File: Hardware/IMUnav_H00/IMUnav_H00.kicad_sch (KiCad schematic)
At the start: 39 parts, among them J1 Conn_01x03_Pin, J2 Conn_01x03_Pin, J3 Conn_01x03_Pin, J4 Conn_01x03_Pin, J5 Conn_01x03_Pin, J6 Conn_01x03_Pin, U1 STM32F446VETx, X1 SX5M24.000M20F30TNN

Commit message: PCB routing
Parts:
- removed J1: Conn_01x03_Pin, Connector_PinHeader_2.54mm:PinHeader_1x03_P2.54mm_Vertical, symbol Connector:Conn_01x03_Pin
- added J10: Conn_ARM_JTAG_SWD_10, Connector_PinHeader_1.27mm:PinHeader_2x05_P1.27mm_Vertical, symbol Connector:Conn_ARM_JTAG_SWD_10
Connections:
- new net: J10.3 (GND), J10.5 (GND)
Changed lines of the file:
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@@
   (junction (at 64.77 106.68) (diameter 0) (color 0 0 0 0)
   )
-  (junction (at 73.66 106.68) (diameter 0) (color 0 0 0 0)
-  )
   (junction (at 203.2 67.31) (diameter 0) (color 0 0 0 0)
   )
@@
   (junction (at 187.96 134.62) (diameter 0) (color 0 0 0 0)
   )
-  (junction (at 71.12 104.14) (diameter 0) (color 0 0 0 0)
-  )
   (junction (at 219.71 35.56) (diameter 0) (color 0 0 0 0)
   )
@@
   (no_connect (at 152.4 158.75))
   (no_connect (at 106.68 80.01))
-  (wire (pts (xy 78.74 93.98) (xy 71.12 93.98))
-    (stroke (width 0) (type default))
-  )
   (wire (pts (xy 276.86 34.29) (xy 276.86 16.51))
     (stroke (width 0) (type default))
@@
     (stroke (width 0) (type default))
   )
-  (wire (pts (xy 73.66 96.52) (xy 73.66 106.68))
-    (stroke (width 0) (type default))
-  )
   (wire (pts (xy 152.4 107.95) (xy 156.21 107.95))
     (stroke (width 0) (type default))
@@
     (stroke (width 0) (type default))
   )
-  (wire (pts (xy 73.66 106.68) (xy 64.77 106.68))
-    (stroke (width 0) (type default))
-  )
   (wire (pts (xy 262.89 88.9) (xy 273.05 88.9))
     (stroke (width 0) (type default))
@@
     (stroke (width 0) (type default))
   )
+  (wire (pts (xy 262.89 49.53) (xy 270.51 49.53))
+    (stroke (width 0) (type default))
+  )
   (wire (pts (xy 198.12 81.28) (xy 203.2 81.28))
     (stroke (width 0) (type default))
@@
     (stroke (width 0) (type default))
   )
-  (wire (pts (xy 71.12 104.14) (xy 76.2 104.14))
-    (stroke (width 0) (type default))
-  )
   (wire (pts (xy 191.77 88.9) (xy 205.74 88.9))
     (stroke (width 0) (type default))
@@
     (stroke (width 0) (type default))
   )
-  (wire (pts (xy 262.89 25.4) (xy 270.51 25.4))
-    (stroke (width 0) (type default))
-  )
   (wire (pts (xy 187.96 134.62) (xy 196.85 134.62))
     (stroke (width 0) (type default))
   )
-  (wire (pts (xy 262.89 49.53) (xy 270.51 49.53))
-    (stroke (width 0) (type default))
-  )
   (wire (pts (xy 220.98 143.51) (xy 224.79 143.51))
     (stroke (width 0) (type default))
   )
-  (wire (pts (xy 71.12 93.98) (xy 71.12 104.14))
-    (stroke (width 0) (type default))
-  )
   (wire (pts (xy 77.47 176.53) (xy 95.25 176.53))
     (stroke (width 0) (type default))
@@
     (stroke (width 0) (type default))
   )
-  (wire (pts (xy 76.2 97.79) (xy 78.74 97.79))
-    (stroke (width 0) (type default))
-  )
   (wire (pts (xy 220.98 99.06) (xy 224.79 99.06))
     (stroke (width 0) (type default))
@@
     (stroke (width 0) (type default))
   )
-  (wire (pts (xy 73.66 106.68) (xy 76.2 106.68))
+  (wire (pts (xy 64.77 106.68) (xy 76.2 106.68))
     (stroke (width 0) (type default))
   )
@@
     (stroke (width 0) (type default))
   )
-  (wire (pts (xy 71.12 104.14) (xy 57.15 104.14))
-    (stroke (width 0) (type default))
-  )
-  (wire (pts (xy 78.74 97.79) (xy 78.74 99.06))
+  (wire (pts (xy 57.15 104.14) (xy 76.2 104.14))
     (stroke (width 0) (type default))
   )
@@
     (stroke (width 0) (type default))
   )
-  (wire (pts (xy 78.74 96.52) (xy 73.66 96.52))
-    (stroke (width 0) (type default))
-  )
   (wire (pts (xy 121.92 13.97) (xy 121.92 31.75))
     (stroke (width 0) (type default))
@@
     (stroke (width 0) (type default))
   )
+  (wire (pts (xy 262.89 52.07) (xy 267.97 52.07))
+    (stroke (width 0) (type default))
+  )
   (wire (pts (xy 190.5 132.08) (xy 185.42 132.08))
     (stroke (width 0) (type default))
@@
     (stroke (width 0) (type default))
   )
-  (wire (pts (xy 262.89 27.94) (xy 270.51 27.94))
-    (stroke (width 0) (type default))
-  )
   (wire (pts (xy 102.87 135.89) (xy 106.68 135.89))
     (stroke (width 0) (type default))
@@
     (stroke (width 0) (type default))
   )
+  (wire (pts (xy 262.89 27.94) (xy 270.51 27.94))
+    (stroke (width 0) (type default))
+  )
   (wire (pts (xy 152.4 46.99) (xy 156.21 46.99))
     (stroke (width 0) (type default))
@@
     (stroke (width 0) (type default))
   )
+  (wire (pts (xy 262.89 25.4) (xy 270.51 25.4))
+    (stroke (width 0) (type default))
+  )
   (wire (pts (xy 152.4 52.07) (xy 156.21 52.07))
     (stroke (width 0) (type default))
@@
     (stroke (width 0) (type default))
   )
-  (wire (pts (xy 267.97 52.07) (xy 262.89 52.07))
-    (stroke (width 0) (type default))
-  )
   (wire (pts (xy 203.2 38.1) (xy 200.66 38.1))
     (stroke (width 0) (type default))
@@
     )
   )
+  (symbol (lib_id "Connector:Conn_ARM_JTAG_SWD_10") (at -77.47 142.24 0) (unit 1)
+    (in_bom yes) (on_board yes) (dnp no) (fields_autoplaced)
+    (property "Reference" "J10" (at -88.3919 141.0279 0)
+      (effects (font (size 1.27 1.27)) (justify right))
+    )
+    (property "Value" "Conn_ARM_JTAG_SWD_10" (at -88.3919 143.4521 0)
+      (effects (font (size 1.27 1.27)) (justify right))
+    )
+    (property "Footprint" "Connector_PinHeader_1.27mm:PinHeader_2x05_P1.27mm_Vertical" (at -77.47 142.24 0)
+      (effects (font (size 1.27 1.27)) hide)
+    )
+    (property "Datasheet" "http://infocenter.arm.com/help/topic/com.arm.doc.ddi0314h/DDI0314H_coresight_components_trm.pdf" (at -86.36 173.99 90)
+      (effects (font (size 1.27 1.27)) hide)
+    )
+    (pin "9")
+    (pin "2")
+    (pin "4")
+    (pin "7")
+    (pin "8")
+    (pin "10")
+    (pin "1")
+    (pin "3")
+    (pin "5")
+    (pin "6")
+    (instances
+      (project "IMUnav_H00"
+        (path "/4c2dd95e-3649-4040-ab57-00df6d22e0b0"
+          (reference "J10") (unit 1)
+        )
+      )
+    )
+  )
   (symbol (lib_id "Device:R") (at 204.47 127 0) (mirror y) (unit 1)
     (in_bom yes) (on_board yes) (dnp no)
@@
     )
   )
-  (symbol (lib_id "power:GND") (at 76.2 97.79 0) (mirror y) (unit 1)
-    (in_bom yes) (on_board yes) (dnp no)
-    (property "Reference" "#PWR023" (at 76.2 104.14 0)
-      (effects (font (size 1.27 1.27)) hide)
-    )
-    (property "Value" "GND" (at 76.073 102.1842 0)
-      (effects (font (size 1.27 1.27)))
-    )
-    (property "Footprint" "" (at 76.2 97.79 0)
-      (effects (font (size 1.27 1.27)) hide)
-    )
-    (property "Datasheet" "" (at 76.2 97.79 0)
-      (effects (font (size 1.27 1.27)) hide)
-    )
-    (pin "1")
-    (instances
-      (project "IMUnav_H00"
-        (path "/4c2dd95e-3649-4040-ab57-00df6d22e0b0"
-          (reference "#PWR023") (unit 1)
-        )
-      )
-      (project "PaLampa_MoBo_H01"
-        (path "/68867493-9f89-4388-916e-56f5ada0ac5c"
-          (reference "#PWR?") (unit 1)
-        )
-      )
-    )
-  )
   (symbol (lib_id "Device:R") (at 64.77 97.79 0) (unit 1)
     (in_bom yes) (on_board yes) (dnp no)
@@
     )
   )
-  (symbol (lib_id "Connector:Conn_01x03_Pin") (at 83.82 96.52 0) (mirror y) (unit 1)
-    (in_bom yes) (on_board yes) (dnp no)
-    (property "Reference" "J1" (at 83.185 89.7595 0)
-      (effects (font (size 1.27 1.27)))
-    )
-    (property "Value" "Conn_01x03_Pin" (at 77.47 91.44 0)
-      (effects (font (size 1.27 1.27)))
-    )
-    (property "Footprint" "Connector_PinHeader_2.54mm:PinHeader_1x03_P2.54mm_Vertical" (at 83.82 96.52 0)
-      (effects (font (size 1.27 1.27)) hide)
-    )
-    (property "Datasheet" "~" (at 83.82 96.52 0)
-      (effects (font (size 1.27 1.27)) hide)
-    )
-    (pin "1")
-    (pin "2")
-    (pin "3")
-    (instances
-      (project "IMUnav_H00"
-        (path "/4c2dd95e-3649-4040-ab57-00df6d22e0b0"
-          (reference "J1") (unit 1)
-        )
-      )
-    )
-  )
   (symbol (lib_id "Device:C") (at 41.91 161.29 0) (unit 1)
     (in_bom yes) (on_board yes) (dnp no)
@@
       (effects (font (size 1.27 1.27)) (justify right))
     )
-    (pin "USB1_D+" input (at 262.89 49.53 0)
+    (pin "USB1_D+" input (at 262.89 25.4 0)
       (effects (font (size 1.27 1.27)) (justify right))
     )
-    (pin "USB1_D-" input (at 262.89 52.07 0)
+    (pin "USB1_D-" input (at 262.89 27.94 0)
       (effects (font (size 1.27 1.27)) (justify right))
     )
-    (pin "USB4_D-" input (at 262.89 27.94 0)
+    (pin "USB4_D-" input (at 262.89 52.07 0)
       (effects (font (size 1.27 1.27)) (justify right))
     )
-    (pin "USB4_D+" input (at 262.89 25.4 0)
+    (pin "USB4_D+" input (at 262.89 49.53 0)
       (effects (font (size 1.27 1.27)) (justify right))
     )

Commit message: PCB routing
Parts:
- removed SWD1: Conn_01x06_Pin, Connector_PinHeader_2.54mm:PinHeader_1x06_P2.54mm_Vertical, symbol Connector:Conn_01x06_Pin
- added RESET2: SW_SPST, Button_Switch_SMD:SW_SPST_TL3342, symbol Switch:SW_SPST
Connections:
- net +3V3: now also J10.1 (VTref)
- net GND: now also J10.3 (GND), J10.5 (GND), J10.9 (GNDDetect), RESET2.1 (A)
- net SWD_CLK: now also J10.4 (SWCLK/TCK)
- net SWD_NRST: now also J10.10 (~{RESET}), RESET2.2 (B)
- net SWD_SWIO: now also J10.2 (SWDIO/TMS)
- net SWD_SWO: now also J10.6 (SWO/TDO)
- no-connect marks 21 -> 22
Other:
- moved on the sheet: J10

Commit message: Silkscreen layout
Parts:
- added G1: FEEC_logo, IMUnav:FEEC_logo, symbol IMUnav:FEEC_logo
- added G2: FEEC_logo_long, IMUnav:FEEC_logo_long, symbol IMUnav:FEEC_logo_long
- renumbered J10 to J1, RESET2 to RESET1

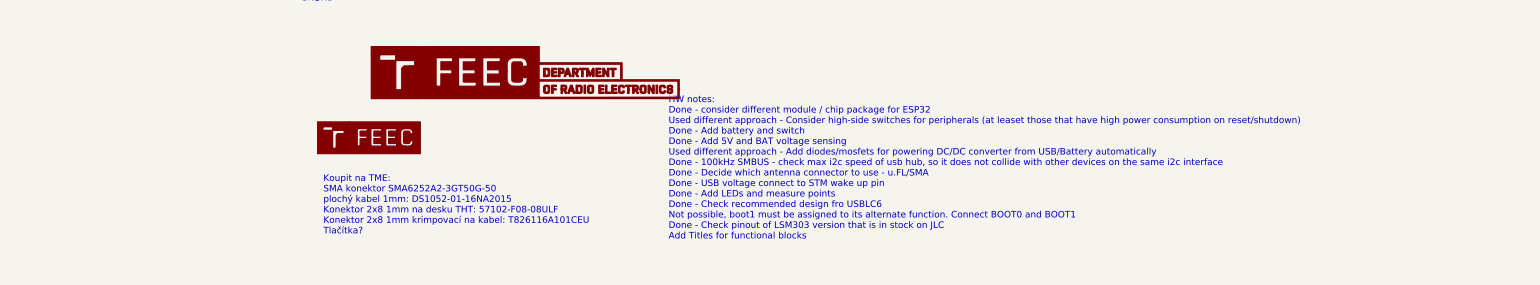
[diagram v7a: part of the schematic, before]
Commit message: PCB touch-ups, bom file for testing
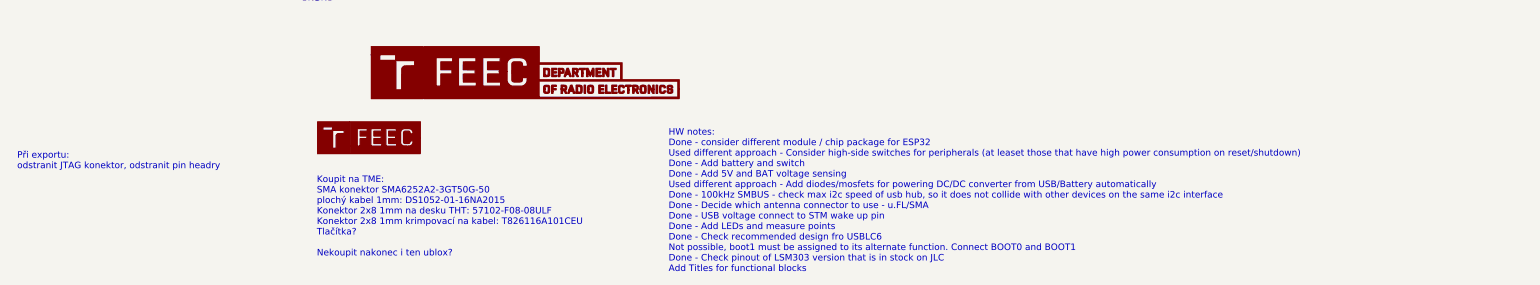
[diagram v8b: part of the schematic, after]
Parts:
- J1, J2, J3, J4, J5, J6: now left out of the parts list
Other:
- note added: "Koupit na TME: SMA konektor SMA6252A2-3GT50G-50 plochý kabel 1mm: DS1052-01-16NA2015 Konektor 2x8 1mm na desku THT: 57102-F08-08ULF Konektor 2x8 1mm krimpovací na kabel: T826116A101CEU Tlačítka? Nekoupit nakonec i ten ublox?"
- note added: "Při exportu: odstranit JTAG konektor, odstranit pin headry"
- note removed: "Koupit na TME: SMA konektor SMA6252A2-3GT50G-50 plochý kabel 1mm: DS1052-01-16NA2015 Konektor 2x8 1mm na desku THT: 57102-F08-08ULF Konektor 2x8 1mm krimpovací na kabel: T826116A101CEU Tlačítka?"
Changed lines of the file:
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@@
     (stroke (width 0) (type default))
   )
+  (text "Při exportu:\nodstranit JTAG konektor, odstranit pin headry"
+    (at 15.24 229.87 0)
+    (effects (font (size 1.27 1.27)) (justify left bottom))
+  )
   (text "HW notes:\nDone - consider different module / chip package for ESP32\nUsed different approach - Consider high-side switches for peripherals (at leaset those that have high power consumption on reset/shutdown)\nDone - Add battery and switch\nDone - Add 5V and BAT voltage sensing\nUsed different approach - Add diodes/mosfets for powering DC/DC converter from USB/Battery automatically\nDone - 100kHz SMBUS - check max i2c speed of usb hub, so it does not collide with other devices on the same i2c interface\nDone - Decide which antenna connector to use - u.FL/SMA\nDone - USB voltage connect to STM wake up pin\nDone - Add LEDs and measure points\nDone - Check recommended design fro USBLC6\nNot possible, boot1 must be assigned to its alternate function. Connect BOOT0 and BOOT1\nDone - Check pinout of LSM303 version that is in stock on JLC\nAdd Titles for functional blocks\n\n\n"
-    (at 142.24 247.65 0)
+    (at 142.24 254 0)
     (effects (font (size 1.27 1.27)) (justify left bottom))
   )
-  (text "Koupit na TME:\nSMA konektor SMA6252A2-3GT50G-50\nplochý kabel 1mm: DS1052-01-16NA2015\nKonektor 2x8 1mm na desku THT: 57102-F08-08ULF\nKonektor 2x8 1mm krimpovací na kabel: T826116A101CEU\nTlačítka?\n"
-    (at 74.93 242.57 0)
+  (text "Koupit na TME:\nSMA konektor SMA6252A2-3GT50G-50\nplochý kabel 1mm: DS1052-01-16NA2015\nKonektor 2x8 1mm na desku THT: 57102-F08-08ULF\nKonektor 2x8 1mm krimpovací na kabel: T826116A101CEU\nTlačítka?\n\nNekoupit nakonec i ten ublox?\n\n"
+    (at 73.66 248.92 0)
     (effects (font (size 1.27 1.27)) (justify left bottom))
   )
@@
   )
   (symbol (lib_id "Connector:Conn_ARM_JTAG_SWD_10") (at 74.93 176.53 0) (unit 1)
-    (in_bom yes) (on_board yes) (dnp no)
+    (in_bom no) (on_board yes) (dnp no)
     (property "Reference" "J1" (at 92.71 182.88 0)
       (effects (font (size 1.27 1.27)) (justify right))
@@
   )
   (symbol (lib_id "Connector:Conn_01x03_Pin") (at 193.04 106.68 0) (unit 1)
-    (in_bom yes) (on_board yes) (dnp no) (fields_autoplaced)
+    (in_bom no) (on_board yes) (dnp no) (fields_autoplaced)
     (property "Reference" "J6" (at 193.675 99.9195 0)
       (effects (font (size 1.27 1.27)))
@@
   )
   (symbol (lib_id "Connector:Conn_01x03_Pin") (at 177.8 124.46 0) (unit 1)
-    (in_bom yes) (on_board yes) (dnp no) (fields_autoplaced)
+    (in_bom no) (on_board yes) (dnp no) (fields_autoplaced)
     (property "Reference" "J2" (at 178.435 117.6995 0)
       (effects (font (size 1.27 1.27)))
@@
   )
   (symbol (lib_id "Connector:Conn_01x03_Pin") (at 193.04 27.94 0) (unit 1)
-    (in_bom yes) (on_board yes) (dnp no) (fields_autoplaced)
+    (in_bom no) (on_board yes) (dnp no) (fields_autoplaced)
     (property "Reference" "J3" (at 193.675 21.1795 0)
       (effects (font (size 1.27 1.27)))
@@
   )
   (symbol (lib_id "Connector:Conn_01x03_Pin") (at 193.04 81.28 0) (unit 1)
-    (in_bom yes) (on_board yes) (dnp no) (fields_autoplaced)
+    (in_bom no) (on_board yes) (dnp no) (fields_autoplaced)
     (property "Reference" "J5" (at 193.675 74.5195 0)
       (effects (font (size 1.27 1.27)))
@@
   )
   (symbol (lib_id "Connector:Conn_01x03_Pin") (at 193.04 57.15 0) (unit 1)
-    (in_bom yes) (on_board yes) (dnp no) (fields_autoplaced)
+    (in_bom no) (on_board yes) (dnp no) (fields_autoplaced)
     (property "Reference" "J4" (at 193.675 50.3895 0)
       (effects (font (size 1.27 1.27)))
